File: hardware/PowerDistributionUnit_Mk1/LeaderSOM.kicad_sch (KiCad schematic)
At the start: 14 parts, among them J10 Logic Analyzer, J11 Logic Analyzer, J12 Logic Analyzer, U1 LeaderSOM

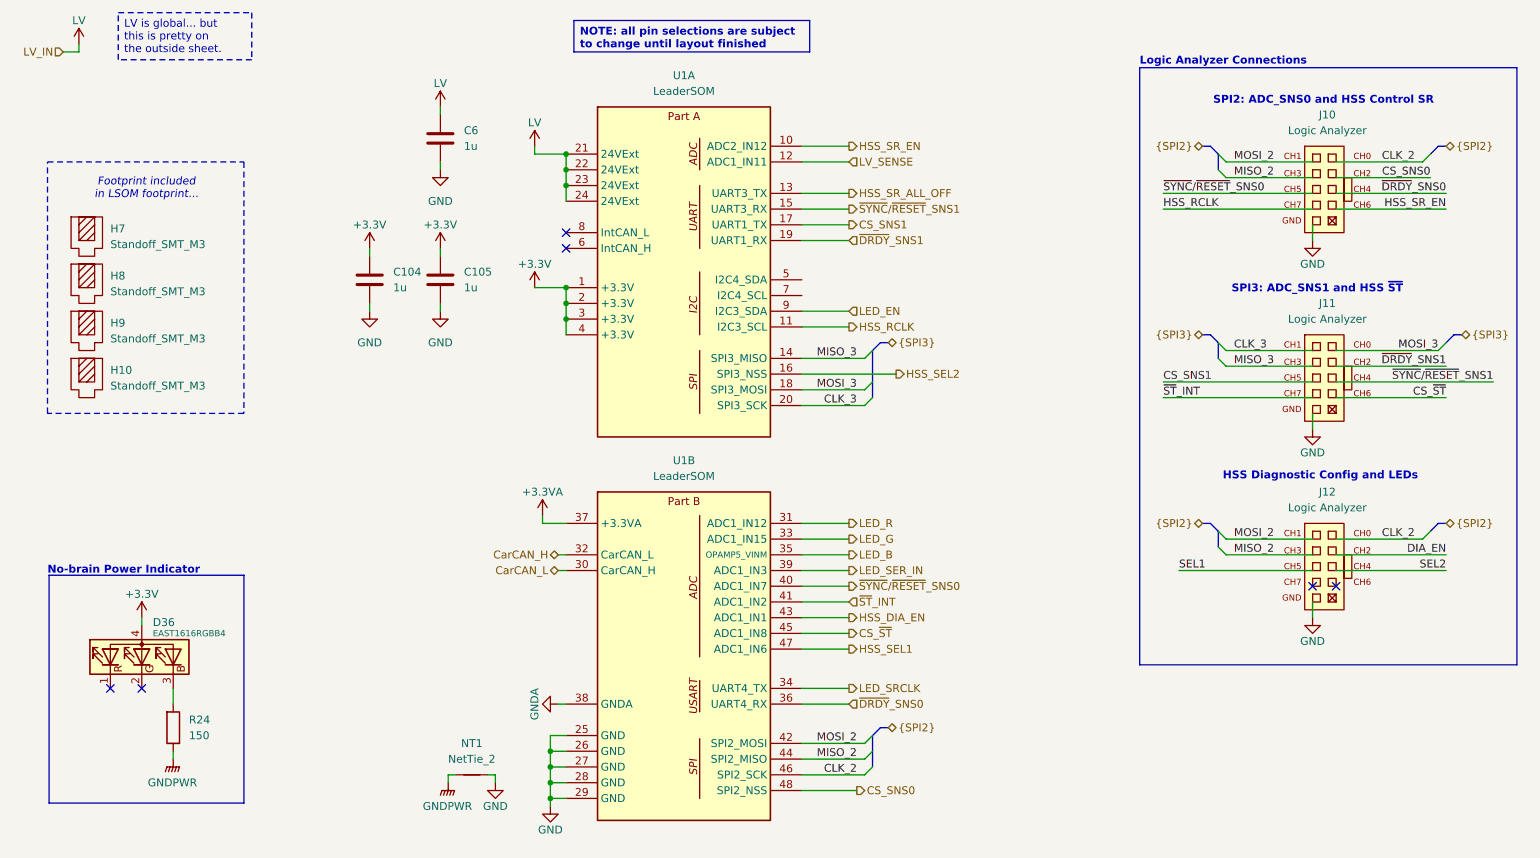
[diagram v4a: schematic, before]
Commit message: move ST GPIO expander into place, route some ADC analog reference/power traces to LSOM, rearrange some GPIO pins
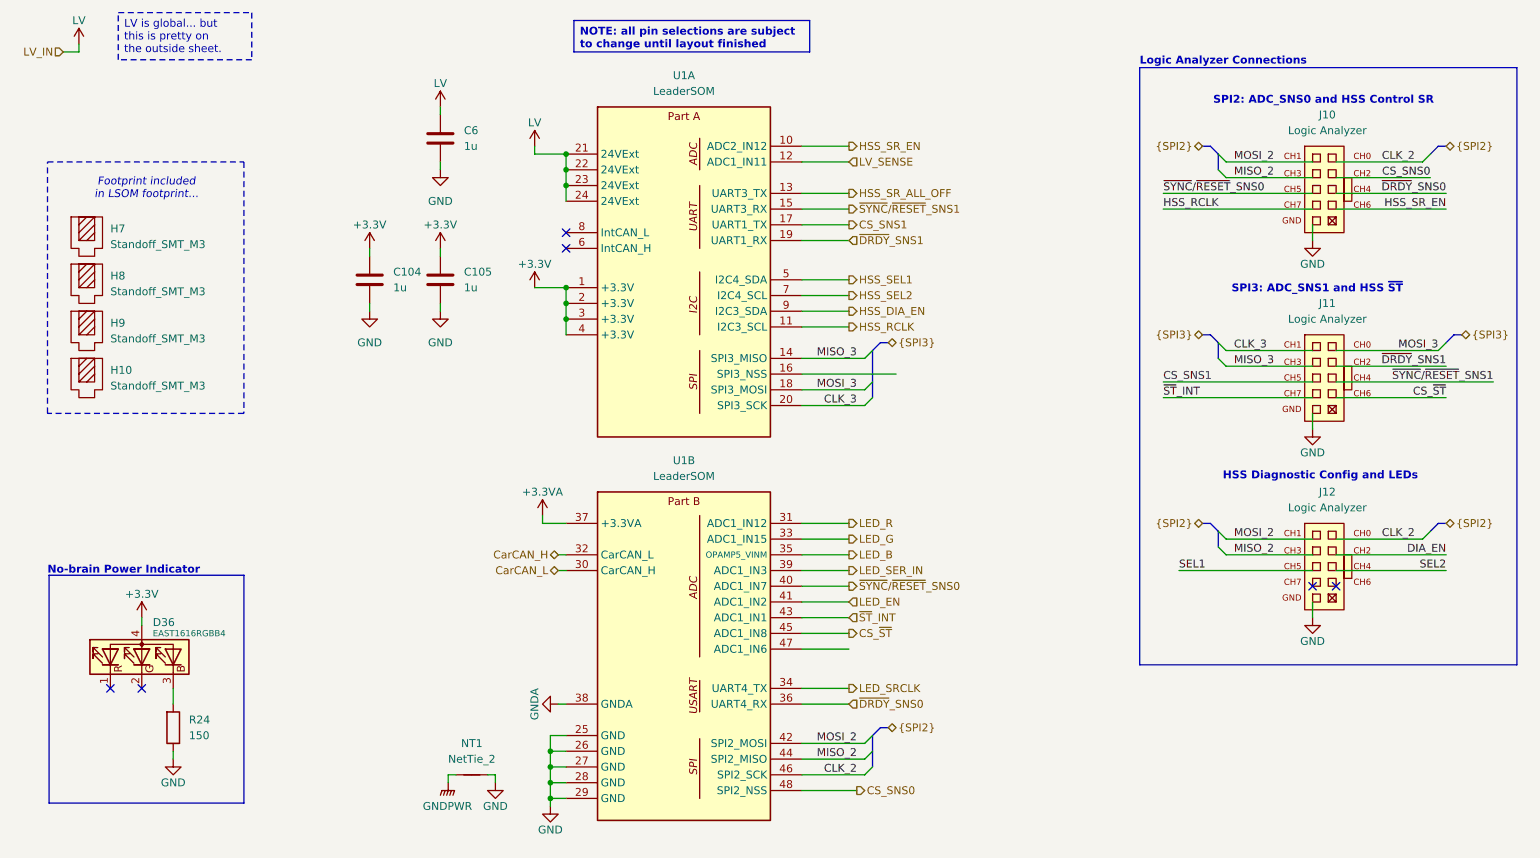
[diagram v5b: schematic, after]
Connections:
- net GND: now also R24.2
- net GNDPWR: no longer R24.2
- net HSS_DIA_EN: now also U1.9 (I2C3_SDA); no longer U1.43 (ADC1_IN1)
- net HSS_SEL1: now also U1.5 (I2C4_SDA); no longer U1.47 (ADC1_IN6)
- net HSS_SEL2: now also U1.7 (I2C4_SCL); no longer U1.16 (SPI3_NSS)
- net LED_EN: now also U1.41 (ADC1_IN2); no longer U1.9 (I2C3_SDA)
- net ~{ST}_INT: now also U1.43 (ADC1_IN1); no longer U1.41 (ADC1_IN2)
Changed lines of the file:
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@@
+	(wire
+		(pts
+			(xy 165.1 66.04) (xy 157.48 66.04)
+		)
+		(stroke
+			(width 0)
+			(type default)
+		)
+	)
 	(wire
 		(pts
@@
 		(pts
 			(xy 157.48 46.99) (xy 165.1 46.99)
+		)
+		(stroke
+			(width 0)
+			(type default)
+		)
+	)
+	(wire
+		(pts
+			(xy 157.48 68.58) (xy 165.1 68.58)
 		)
 		(stroke
@@
 	(hierarchical_label "HSS_DIA_EN"
 		(shape output)
-		(at 165.1 120.65 0)
+		(at 165.1 71.12 0)
 		(effects
 			(font
@@
 	(hierarchical_label "HSS_SEL2"
 		(shape output)
-		(at 172.72 81.28 0)
+		(at 165.1 68.58 0)
 		(effects
 			(font
@@
 	(hierarchical_label "~{ST}_INT"
 		(shape input)
-		(at 165.1 118.11 0)
+		(at 165.1 120.65 0)
 		(effects
 			(font
@@
 	(hierarchical_label "LED_EN"
 		(shape input)
-		(at 165.1 71.12 0)
+		(at 165.1 118.11 0)
 		(effects
 			(font
@@
 	(hierarchical_label "HSS_SEL1"
 		(shape output)
-		(at 165.1 125.73 0)
+		(at 165.1 66.04 0)
 		(effects
 			(font
@@
 	)
 	(symbol
-		(lib_id "power:GNDPWR")
-		(at 55.88 143.51 0)
-		(unit 1)
-		(exclude_from_sim no)
-		(in_bom yes)
-		(on_board yes)
-		(dnp no)
-		(fields_autoplaced yes)
-		(property "Reference" "#PWR064"
-			(at 55.88 148.59 0)
-			(effects
-				(font
-					(size 1.27 1.27)
-				)
-				(hide yes)
-			)
-		)
-		(property "Value" "GNDPWR"
-			(at 55.753 147.32 0)
-			(effects
-				(font
-					(size 1.27 1.27)
-				)
-			)
-		)
-		(property "Footprint" ""
-			(at 55.88 144.78 0)
-			(effects
-				(font
-					(size 1.27 1.27)
-				)
-				(hide yes)
-			)
-		)
-		(property "Datasheet" ""
-			(at 55.88 144.78 0)
-			(effects
-				(font
-					(size 1.27 1.27)
-				)
-				(hide yes)
-			)
-		)
-		(property "Description" "Power symbol creates a global label with name \"GNDPWR\" , global ground"
-			(at 55.88 143.51 0)
-			(effects
-				(font
-					(size 1.27 1.27)
-				)
-				(hide yes)
-			)
-		)
-		(pin "1"
-		)
-		(instances
-			(project "PowerDistributionUnit_Mk1"
-				(path "/6abaf095-8ba7-4306-8425-59a9eb37aa2b/9db45747-239d-4a98-a456-ca77cdc3d84b"
-					(reference "#PWR064")
-					(unit 1)
-				)
-			)
-		)
-	)
-	(symbol
 		(lib_id "power:GND")
 		(at 116.84 151.13 0)
@@
 					(unit 1)
 				)
+			)
+		)
+	)
+	(symbol
+		(lib_id "power:GND")
+		(at 55.88 143.51 0)
+		(unit 1)
+		(exclude_from_sim no)
+		(in_bom yes)
+		(on_board yes)
+		(dnp no)
+		(property "Reference" "#PWR087"
+			(at 55.88 149.86 0)
+			(effects
+				(font
+					(size 1.27 1.27)
+				)
+				(hide yes)
+			)
+		)
+		(property "Value" "GND"
+			(at 55.88 147.32 0)
+			(effects
+				(font
+					(size 1.27 1.27)
+				)
+			)
+		)
+		(property "Footprint" ""
+			(at 55.88 143.51 0)
+			(effects
+				(font
+					(size 1.27 1.27)
+				)
+				(hide yes)
+			)
+		)
+		(property "Datasheet" ""
+			(at 55.88 143.51 0)
+			(effects
+				(font
+					(size 1.27 1.27)
+				)
+				(hide yes)
+			)
+		)
+		(property "Description" "Power symbol creates a global label with name \"GND\" , ground"
+			(at 55.88 143.51 0)
+			(effects
+				(font
+					(size 1.27 1.27)
+				)
+				(hide yes)
+			)
+		)
+		(pin "1"
+		)
+		(instances
+			(project "PowerDistributionUnit_Mk1"
+				(path "/6abaf095-8ba7-4306-8425-59a9eb37aa2b/9db45747-239d-4a98-a456-ca77cdc3d84b"
+					(reference "#PWR087")
+					(unit 1)
+				)

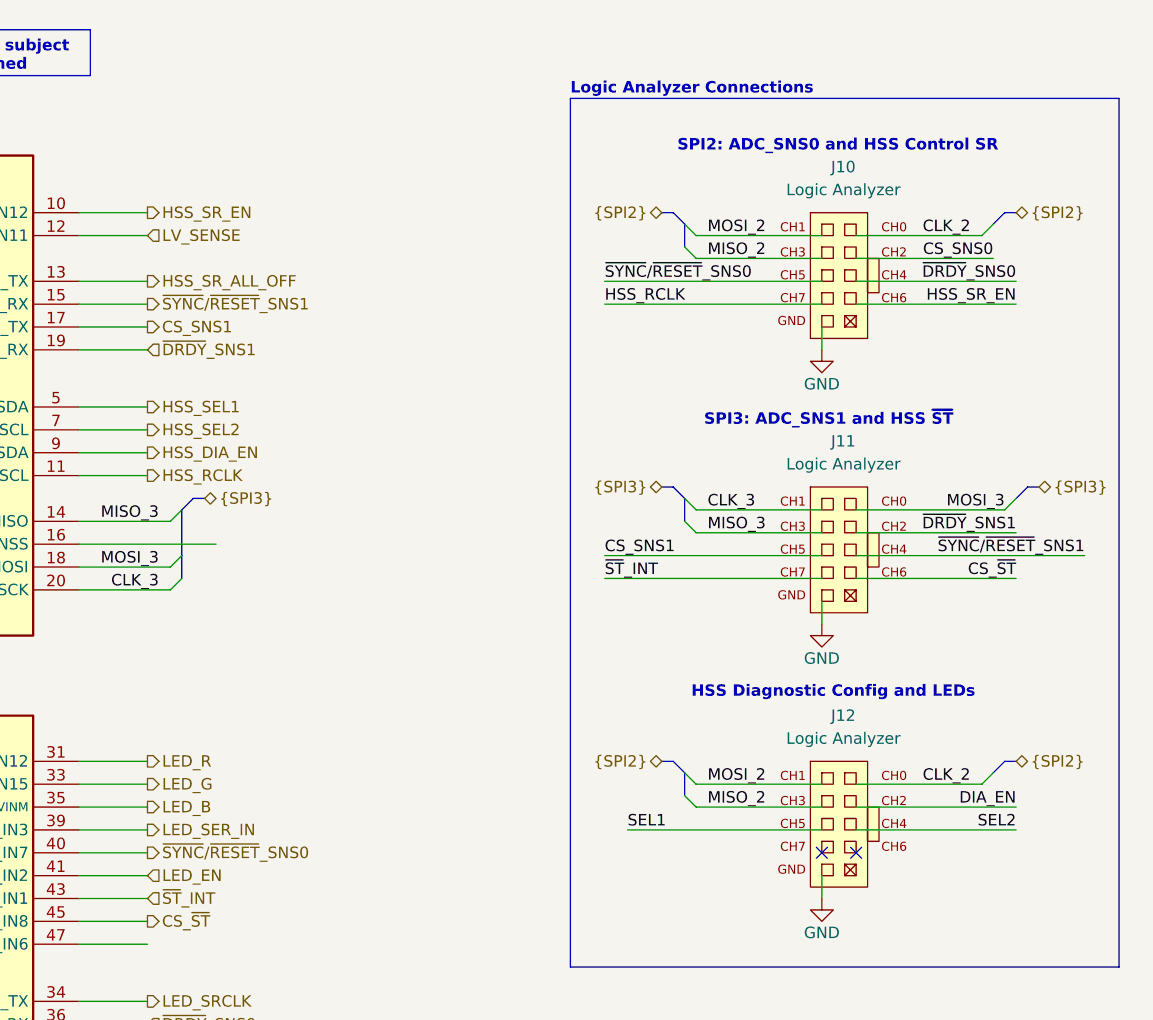
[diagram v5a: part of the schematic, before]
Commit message: routed a couple of logic analyzer connectors, fixed HSS SR out clk label, adjusted logic analyzer pinout
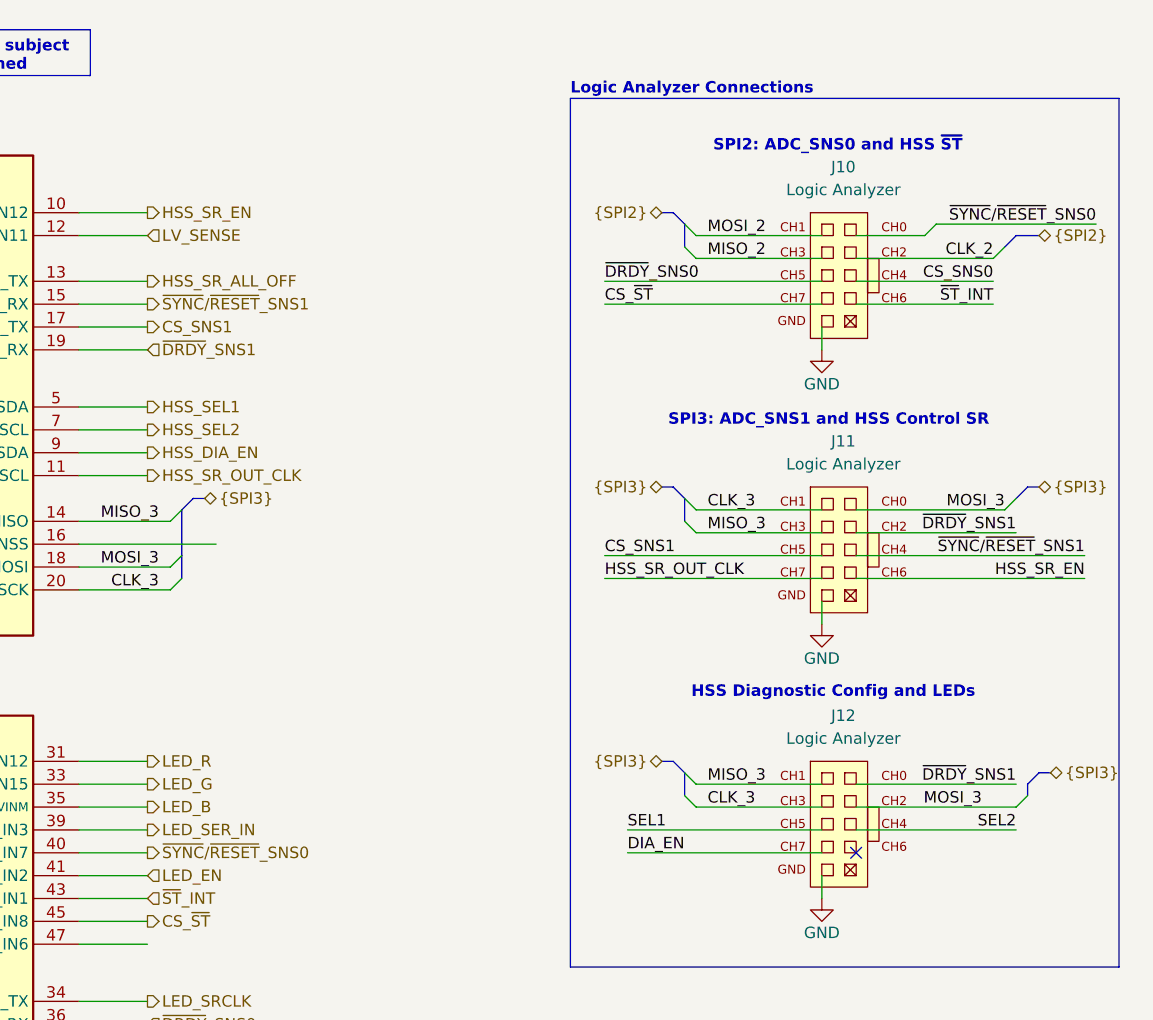
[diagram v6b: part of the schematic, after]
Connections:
- net CLK_2: now also J10.8 (CH2); no longer J10.10 (CH0), J12.10 (CH0)
- net CLK_3: now also J12.7 (CH3)
- net CS_SNS0: now also J10.6 (CH4); no longer J10.8 (CH2)
- net CS_~{ST}: now also J10.3 (CH7); no longer J11.4 (CH6)
- net DIA_EN: now also J12.3 (CH7); no longer J12.8 (CH2)
- net HSS_SR_EN: now also J11.4 (CH6); no longer J10.4 (CH6)
- net MISO_2: no longer J12.7 (CH3)
- net MISO_3: now also J12.9 (CH1)
- net MOSI_2: no longer J12.9 (CH1)
- net MOSI_3: now also J12.8 (CH2)
- net ~{DRDY}_SNS0: now also J10.5 (CH5); no longer J10.6 (CH4)
- net ~{DRDY}_SNS1: now also J12.10 (CH0)
- net ~{ST}_INT: now also J10.4 (CH6); no longer J11.3 (CH7)
- net ~{SYNC}/~{RESET}_SNS0: now also J10.10 (CH0); no longer J10.5 (CH5)
- net HSS_RCLK renamed HSS_SR_OUT_CLK
- net HSS_SR_OUT_CLK: now also J11.3 (CH7); no longer J10.3 (CH7)
- no-connect marks 6 -> 5
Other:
- note added: "SPI2: ADC_SNS0 and HSS ~{ST}"
- note added: "SPI3: ADC_SNS1 and HSS Control SR"
- note removed: "SPI2: ADC_SNS0 and HSS Control SR"
- note removed: "SPI3: ADC_SNS1 and HSS ~{ST}"
